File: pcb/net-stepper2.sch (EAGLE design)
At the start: 37 parts, among them IC2 CP2104, J1 MICRO-USB, J2 POWER_JACKPTH_LOCK, J3 ENCODER, J4 ENDSTOP2, J5 ENDSTOP1, J6 STEPER, Q1 600mA/40V, Q2 600mA/40V, U1 L6470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

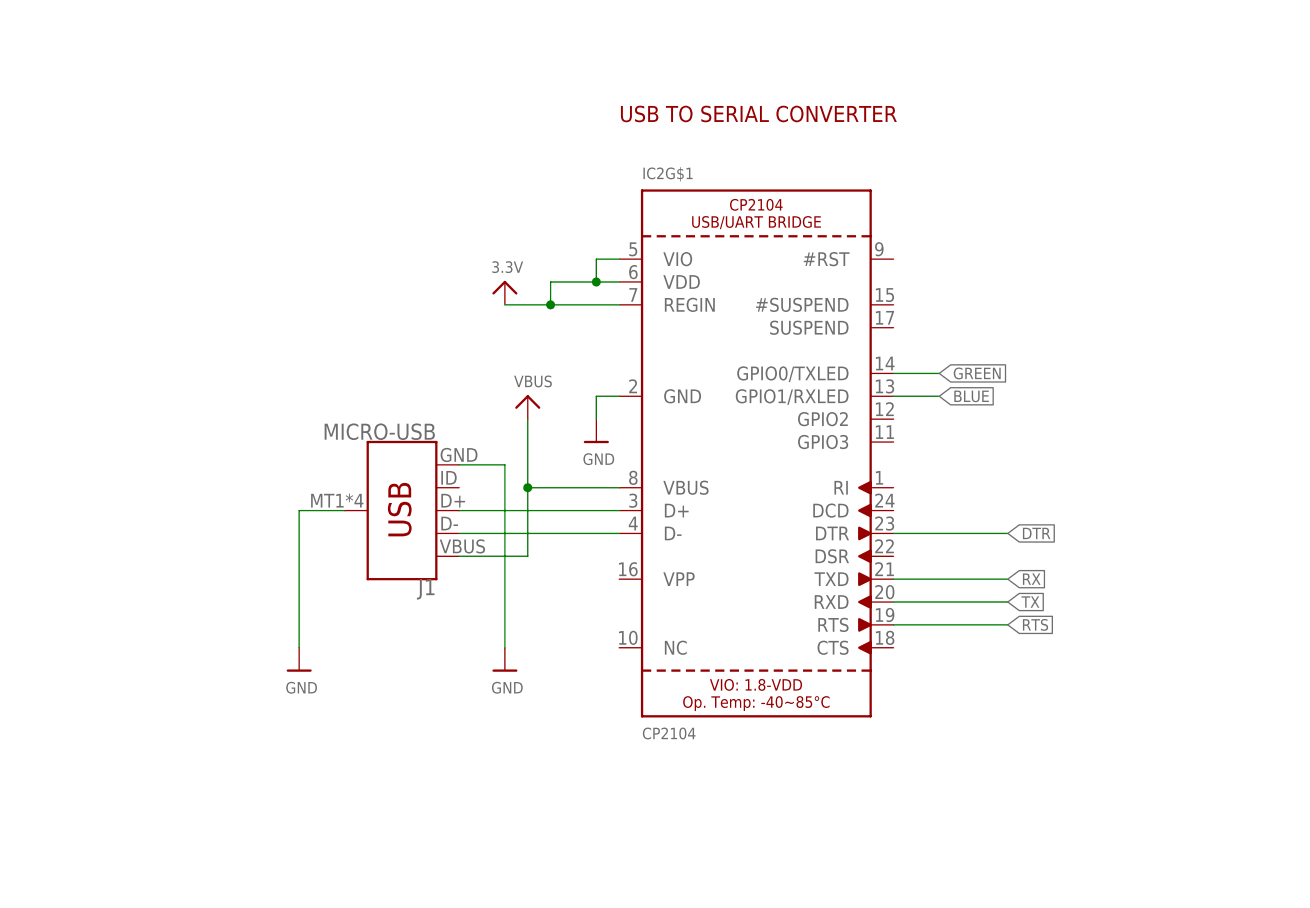
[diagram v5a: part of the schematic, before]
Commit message: replaced cp2104 in order to connect the thermal pad to ground
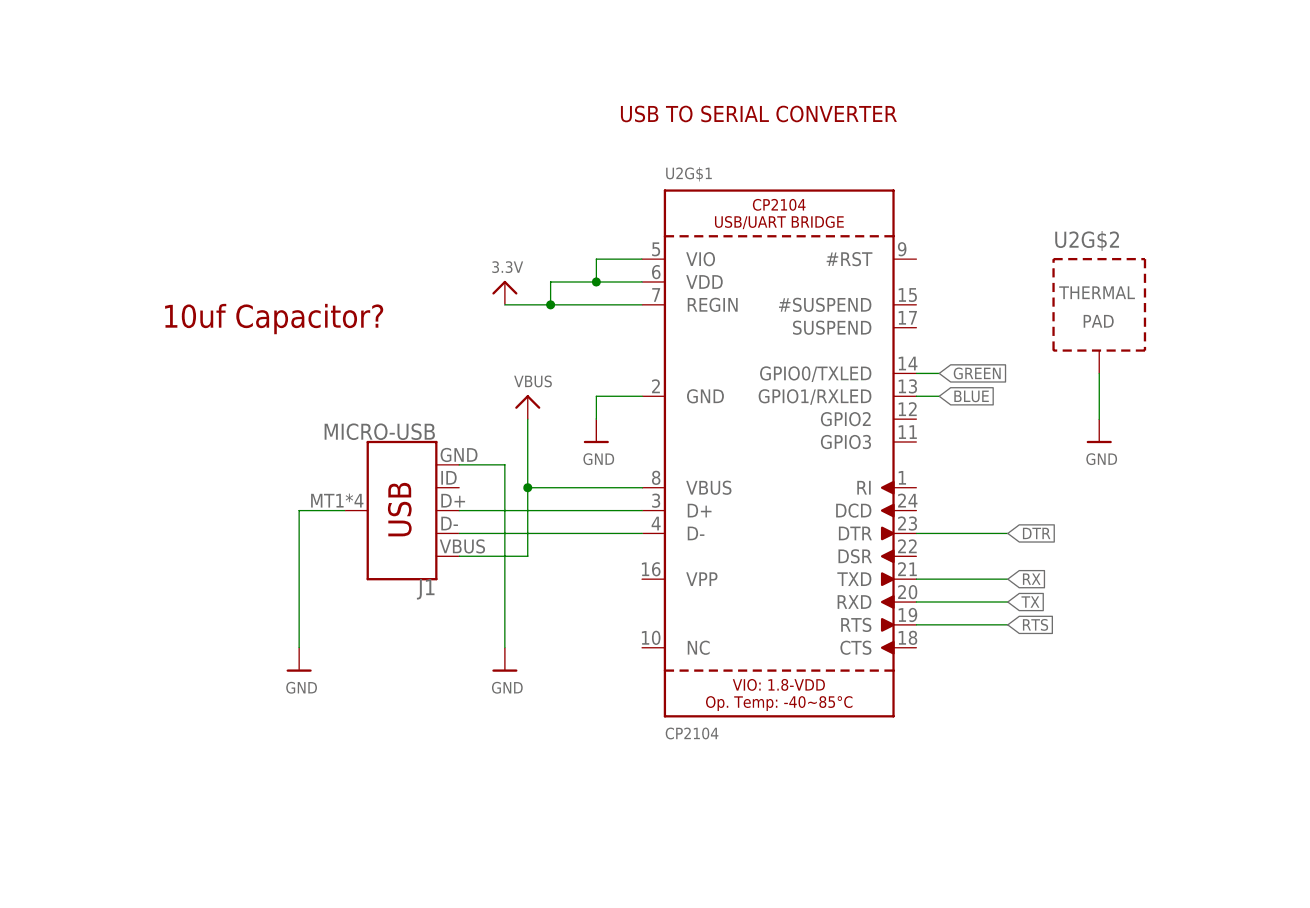
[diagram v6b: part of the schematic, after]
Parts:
- removed IC2: CP2104, microbuilder:CP2104
- added U2: CP2104, microbuilder:CP2104
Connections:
- net 3.3V: now also U2G$1.REGIN, U2G$1.VDD, U2G$1.VIO; no longer IC2G$1.REGIN, IC2G$1.VDD, IC2G$1.VIO
- net BLUE: now also U2G$1.GPIO1/RXLED; no longer IC2G$1.GPIO1/RXLED
- net DTR: now also U2G$1.DTR; no longer IC2G$1.DTR
- net GND: now also U2G$1.GND, U2G$2.TP; no longer IC2G$1.GND
- net GREEN: now also U2G$1.GPIO0/TXLED; no longer IC2G$1.GPIO0/TXLED
- net N$13: now also U2G$1.D+; no longer IC2G$1.D+
- net N$14: now also U2G$1.D-; no longer IC2G$1.D-
- net RTS: now also U2G$1.RTS; no longer IC2G$1.RTS
- net RX: now also U2G$1.TXD; no longer IC2G$1.TXD
- net TX: now also U2G$1.RXD; no longer IC2G$1.RXD
- net VBUS: now also U2G$1.VBUS; no longer IC2G$1.VBUS
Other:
- note added: "10uf Capacitor?"
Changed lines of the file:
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@@
 <part name="S4" library="IAD-Library" deviceset="B3AL-1002P-MS" device=""/>
 <part name="S3" library="IAD-Library" deviceset="B3AL-1002P-MS" device=""/>
-<part name="IC2" library="microbuilder" deviceset="CP2104" device="" value="CP2104"/>
 <part name="U$33" library="microbuilder" deviceset="GND" device=""/>
 <part name="U$34" library="microbuilder" deviceset="GND" device=""/>
@@
 <part name="GND1" library="SparkFun" deviceset="GND" device=""/>
 <part name="U$7" library="microbuilder" deviceset="GND" device=""/>
+<part name="U2" library="microbuilder" deviceset="CP2104" device="" value="CP2104"/>
+<part name="U$16" library="microbuilder" deviceset="GND" device=""/>
 </parts>
 <sheets>
@@
 <text x="474.98" y="157.48" size="1.778" layer="94">USB TO SERIAL CONVERTER</text>
 <text x="205.74" y="25.4" size="1.778" layer="94">RGB LED</text>
+<text x="424.18" y="134.62" size="2.54" layer="94" font="vector" ratio="20">10uf Capacitor?</text>
 </plain>
 <instances>
@@
 <instance part="S4" gate="G$1" x="134.62" y="-2.54"/>
 <instance part="S3" gate="G$1" x="134.62" y="7.62"/>
-<instance part="IC2" gate="G$1" x="490.22" y="121.92"/>
 <instance part="U$33" gate="G$1" x="462.28" y="96.52"/>
 <instance part="U$34" gate="G$1" x="472.44" y="121.92"/>
@@
 <instance part="GND1" gate="1" x="30.48" y="0"/>
 <instance part="U$7" gate="G$1" x="439.42" y="96.52"/>
+<instance part="U2" gate="G$1" x="492.76" y="121.92"/>
+<instance part="U2" gate="G$2" x="528.32" y="137.16"/>
+<instance part="U$16" gate="G$1" x="528.32" y="121.92"/>
 </instances>
 <busses>
@@
 </segment>
 <segment>
-<pinref part="IC2" gate="G$1" pin="GND"/>
 <pinref part="U$34" gate="G$1" pin="GND"/>
-<wire x1="474.98" y1="127" x2="472.44" y2="127" width="0.1524" layer="91"/>
 <wire x1="472.44" y1="127" x2="472.44" y2="124.46" width="0.1524" layer="91"/>
+<pinref part="U2" gate="G$1" pin="GND"/>
+<wire x1="477.52" y1="127" x2="472.44" y2="127" width="0.1524" layer="91"/>
 </segment>
 <segment>
@@
 <pinref part="U$7" gate="G$1" pin="GND"/>
 <wire x1="439.42" y1="99.06" x2="439.42" y2="114.3" width="0.1524" layer="91"/>
+</segment>
+<segment>
+<pinref part="U$16" gate="G$1" pin="GND"/>
+<pinref part="U2" gate="G$2" pin="TP"/>
+<wire x1="528.32" y1="124.46" x2="528.32" y2="129.54" width="0.1524" layer="91"/>
 </segment>
 </net>
@@
 </segment>
 <segment>
-<pinref part="IC2" gate="G$1" pin="REGIN"/>
-<wire x1="474.98" y1="137.16" x2="467.36" y2="137.16" width="0.1524" layer="91"/>
+<wire x1="477.52" y1="137.16" x2="467.36" y2="137.16" width="0.1524" layer="91"/>
 <junction x="467.36" y="137.16"/>
-<pinref part="IC2" gate="G$1" pin="VDD"/>
-<wire x1="474.98" y1="139.7" x2="472.44" y2="139.7" width="0.1524" layer="91"/>
-<pinref part="IC2" gate="G$1" pin="VIO"/>
-<wire x1="474.98" y1="142.24" x2="472.44" y2="142.24" width="0.1524" layer="91"/>
 <wire x1="472.44" y1="142.24" x2="472.44" y2="139.7" width="0.1524" layer="91"/>
 <junction x="472.44" y="139.7"/>
@@
 <wire x1="467.36" y1="137.16" x2="462.28" y2="137.16" width="0.1524" layer="91"/>
 <pinref part="U$38" gate="G$1" pin="3.3V"/>
+<pinref part="U2" gate="G$1" pin="REGIN"/>
+<pinref part="U2" gate="G$1" pin="VDD"/>
+<wire x1="477.52" y1="139.7" x2="472.44" y2="139.7" width="0.1524" layer="91"/>
+<pinref part="U2" gate="G$1" pin="VIO"/>
+<wire x1="477.52" y1="142.24" x2="472.44" y2="142.24" width="0.1524" layer="91"/>
 </segment>
 <segment>
@@
 </segment>
 <segment>
-<pinref part="IC2" gate="G$1" pin="DTR"/>
-<wire x1="505.46" y1="111.76" x2="518.16" y2="111.76" width="0.1524" layer="91"/>
 <label x="518.16" y="111.76" size="1.27" layer="95" xref="yes"/>
+<pinref part="U2" gate="G$1" pin="DTR"/>
+<wire x1="508" y1="111.76" x2="518.16" y2="111.76" width="0.1524" layer="91"/>
 </segment>
 </net>
@@
 </segment>
 <segment>
-<wire x1="518.16" y1="101.6" x2="505.46" y2="101.6" width="0.1524" layer="91"/>
-<pinref part="IC2" gate="G$1" pin="RTS"/>
+<wire x1="518.16" y1="101.6" x2="508" y2="101.6" width="0.1524" layer="91"/>
 <label x="518.16" y="101.6" size="1.27" layer="95" xref="yes"/>
+<pinref part="U2" gate="G$1" pin="RTS"/>
 </segment>
 </net>
 <net name="TX" class="0">
 <segment>
-<pinref part="IC2" gate="G$1" pin="RXD"/>
-<wire x1="505.46" y1="104.14" x2="518.16" y2="104.14" width="0.1524" layer="91"/>
 <label x="518.16" y="104.14" size="1.27" layer="95" xref="yes"/>
+<pinref part="U2" gate="G$1" pin="RXD"/>
+<wire x1="508" y1="104.14" x2="518.16" y2="104.14" width="0.1524" layer="91"/>
 </segment>
 <segment>
@@
 <net name="RX" class="0">
 <segment>
-<pinref part="IC2" gate="G$1" pin="TXD"/>
-<wire x1="505.46" y1="106.68" x2="518.16" y2="106.68" width="0.1524" layer="91"/>
 <label x="518.16" y="106.68" size="1.27" layer="95" xref="yes"/>
+<pinref part="U2" gate="G$1" pin="TXD"/>
+<wire x1="508" y1="106.68" x2="518.16" y2="106.68" width="0.1524" layer="91"/>
 </segment>
 <segment>
@@
 <net name="VBUS" class="0">
 <segment>
-<pinref part="IC2" gate="G$1" pin="VBUS"/>
-<wire x1="464.82" y1="116.84" x2="474.98" y2="116.84" width="0.1524" layer="91"/>
+<wire x1="464.82" y1="116.84" x2="477.52" y2="116.84" width="0.1524" layer="91"/>
 <pinref part="U$36" gate="G$1" pin="VBUS"/>
 <wire x1="464.82" y1="116.84" x2="464.82" y2="124.46" width="0.1524" layer="91"/>
@@
 <wire x1="464.82" y1="109.22" x2="464.82" y2="116.84" width="0.1524" layer="91"/>
 <junction x="464.82" y="116.84"/>
+<pinref part="U2" gate="G$1" pin="VBUS"/>
 </segment>
 </net>
 <net name="N$13" class="0">
 <segment>
-<pinref part="IC2" gate="G$1" pin="D+"/>
 <pinref part="J1" gate="G$1" pin="D+"/>
-<wire x1="457.2" y1="114.3" x2="474.98" y2="114.3" width="0.1524" layer="91"/>
+<wire x1="457.2" y1="114.3" x2="477.52" y2="114.3" width="0.1524" layer="91"/>
+<pinref part="U2" gate="G$1" pin="D+"/>
 </segment>
 </net>
 <net name="N$14" class="0">
 <segment>
-<pinref part="IC2" gate="G$1" pin="D-"/>
 <pinref part="J1" gate="G$1" pin="D-"/>
-<wire x1="457.2" y1="111.76" x2="474.98" y2="111.76" width="0.1524" layer="91"/>
+<wire x1="457.2" y1="111.76" x2="477.52" y2="111.76" width="0.1524" layer="91"/>
+<pinref part="U2" gate="G$1" pin="D-"/>
 </segment>
 </net>
@@
 <segment>
 <label x="510.54" y="129.54" size="1.27" layer="95" xref="yes"/>
-<pinref part="IC2" gate="G$1" pin="GPIO0/TXLED"/>
-<wire x1="505.46" y1="129.54" x2="510.54" y2="129.54" width="0.1524" layer="91"/>
+<pinref part="U2" gate="G$1" pin="GPIO0/TXLED"/>
+<wire x1="508" y1="129.54" x2="510.54" y2="129.54" width="0.1524" layer="91"/>
 </segment>
 <segment>
@@
 <segment>
 <label x="510.54" y="127" size="1.27" layer="95" xref="yes"/>
-<pinref part="IC2" gate="G$1" pin="GPIO1/RXLED"/>
-<wire x1="505.46" y1="127" x2="510.54" y2="127" width="0.1524" layer="91"/>
-</segment>
-<segment>
+<pinref part="U2" gate="G$1" pin="GPIO1/RXLED"/>
+<wire x1="508" y1="127" x2="510.54" y2="127" width="0.1524" layer="91"/>
+</segment>
+<segment>

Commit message: updated schematics
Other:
- note added: "Fix Wrong Pins"
- moved on the sheet: J4
